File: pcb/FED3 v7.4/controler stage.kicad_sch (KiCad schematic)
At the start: 25 parts, among them IC4 RTC PCF8523T, J1 Conn_02x03_Odd_Even, SW2 SPST_TACT-KMR2, U1 ATSAMD21G18A, U4 Adafruit LCD Screen, X1 ClockXtal, X2 uXtal, X4 microsd

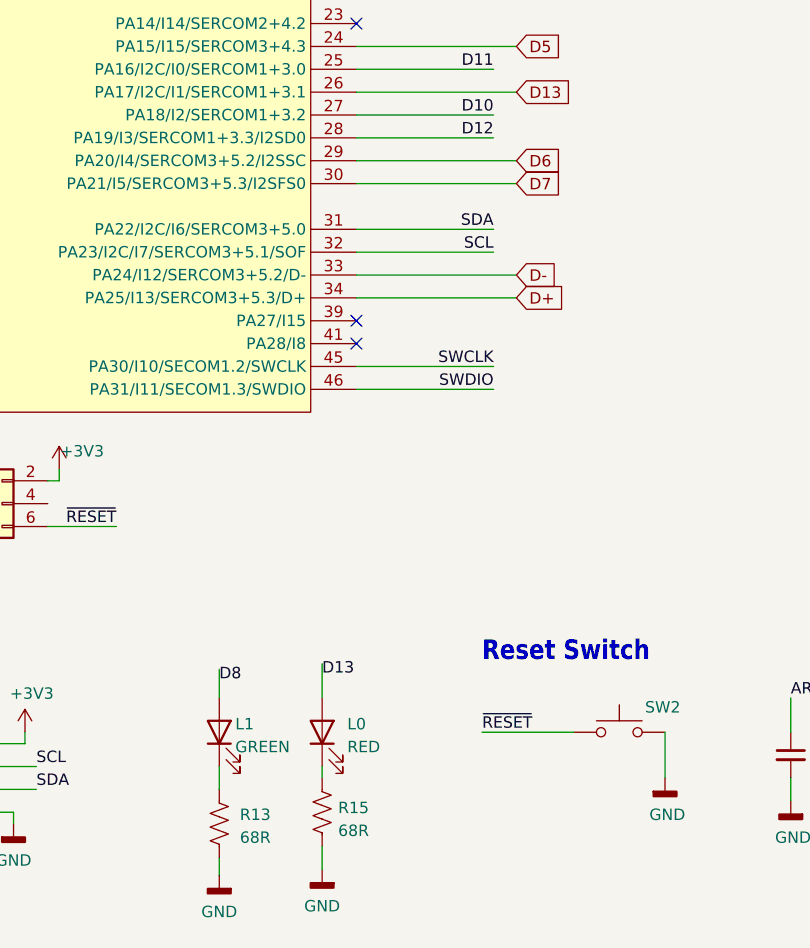
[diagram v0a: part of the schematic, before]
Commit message: v.7.4 - alterações rail power
v.7.4
- modificada estrutura rail power: VUSB apenas para Vcharging
- modificadas Rs de LEDs para diminuir I
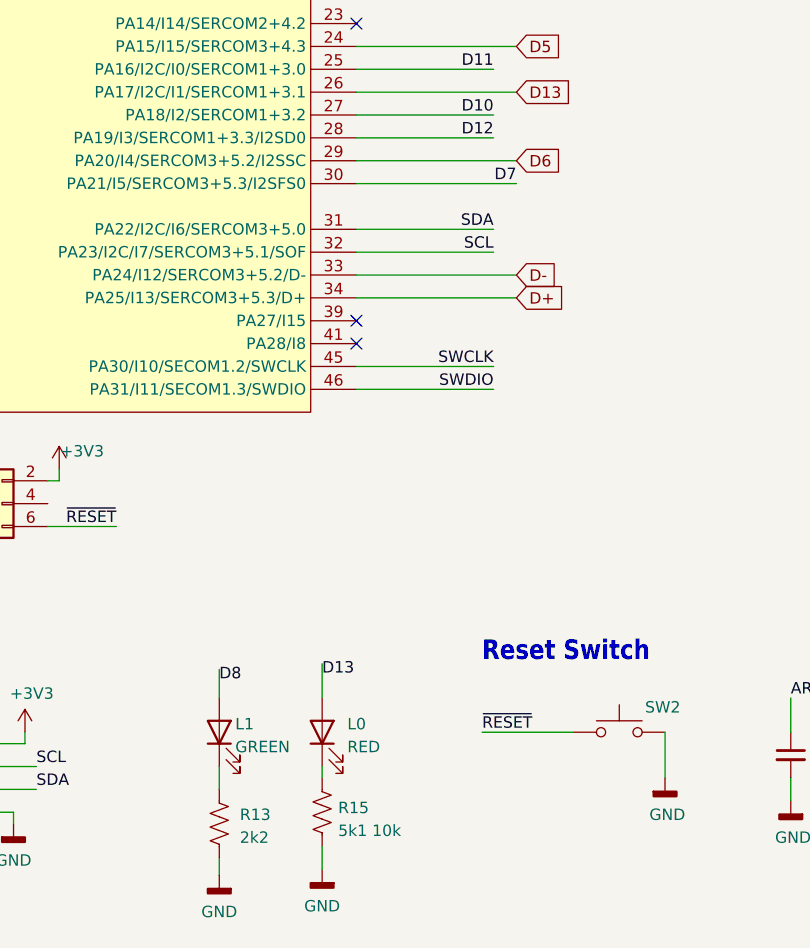
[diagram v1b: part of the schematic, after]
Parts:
- R13: value 68R -> 2k2; MPN RCS040268R0FKED -> ERJ-2RKF2201X; OEPSPN OEPS020032 -> OEPS020174
- R15: value 68R -> 5k1 10k; MPN RCS040268R0FKED -> ??; OEPSPN OEPS020032 -> TBD
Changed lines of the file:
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@@
+		)
+	)
+	(label "D7"
+		(at 138.43 100.33 180)
+		(effects
+			(font
+				(size 1.27 1.27)
+			)
+			(justify right bottom)
 		)
 	)
@@
 		)
 	)
-	(global_label "D7"
-		(shape input)
-		(at 138.43 100.33 0)
-		(fields_autoplaced yes)
-		(effects
-			(font
-				(size 1.27 1.27)
-			)
-			(justify left)
-		)
-		(property "Intersheetrefs" "${INTERSHEET_REFS}"
-			(at 143.7851 100.33 0)
-			(effects
-				(font
-					(size 1.27 1.27)
-				)
-				(justify bottom)
-				(hide yes)
-			)
-		)
-	)
 	(global_label "D6"
 		(shape input)
@@
 			)
 		)
-		(property "Value" "68R"
+		(property "Value" "5k1 10k"
 			(at 118.618 172.974 0)
 			(effects
@@
 			)
 		)
-		(property "OEPSPN" "OEPS020032"
+		(property "OEPSPN" "TBD"
 			(at 116.84 170.18 0)
 			(effects
@@
 			)
 		)
-		(property "MPN" "RCS040268R0FKED"
+		(property "MPN" "??"
 			(at 116.84 170.18 0)
 			(effects
@@
 			)
 		)
-		(property "Value" "68R"
+		(property "Value" "2k2"
 			(at 107.696 173.736 0)
 			(effects
@@
 			)
 		)
-		(property "OEPSPN" "OEPS020032"
+		(property "OEPSPN" "OEPS020174"
 			(at 105.41 171.45 0)
 			(effects
@@
 			)
 		)
-		(property "MPN" "RCS040268R0FKED"
+		(property "MPN" "ERJ-2RKF2201X"
 			(at 105.41 171.45 0)
 			(effects

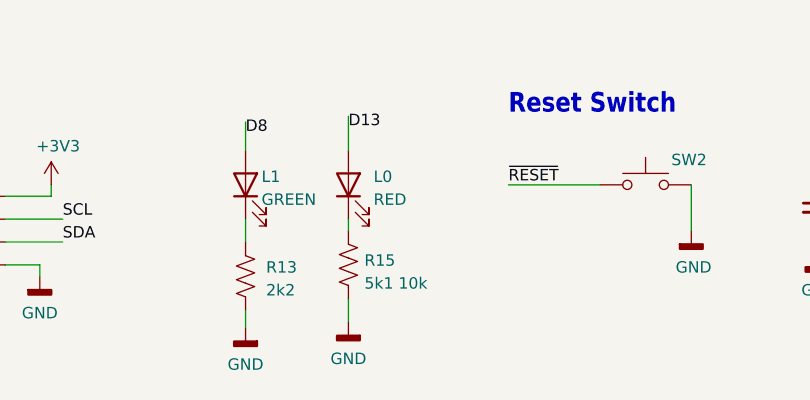
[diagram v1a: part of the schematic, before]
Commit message: v.7.4 - commit to final review
- I2C plug moved to board front side
- Rs to LEDs changed - impose less I
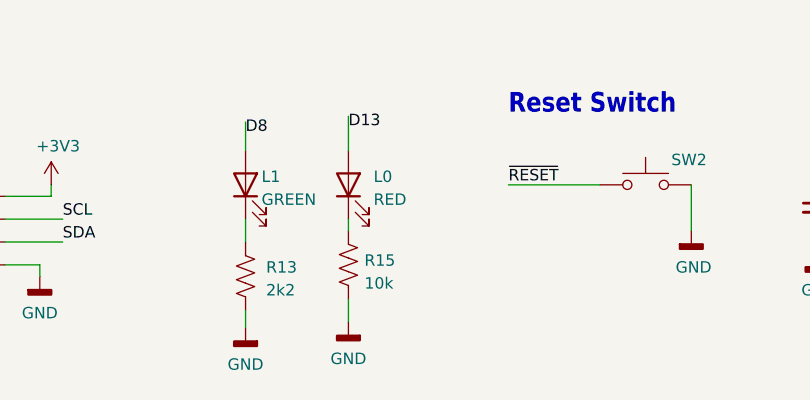
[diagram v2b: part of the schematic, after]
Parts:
- AUX_I2C0: footprint FED3_PCBLib:1X04 -> Connector_JST:JST_PH_B4B-PH-K_1x04_P2.00mm_Vertical
- R15: value 5k1 10k -> 10k; OEPSPN TBD -> OEPS020013
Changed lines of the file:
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@@
 			)
 		)
-		(property "Description" "Two pin crystal"
+		(property "Description" "Crystal 32768 KHz ±50ppm 12.5pF 90kOhms"
 			(at 130.81 39.37 0)
 			(effects
@@
 			)
 		)
-		(property "Description" ""
+		(property "Description" "SMD CER 0402 22pF 50V ±5% C0G/NP0"
 			(at 135.89 29.21 0)
 			(effects
@@
 			)
 		)
-		(property "Description" "32.768 kHz ±10ppm Crystal 12.5pF 50 kOhms"
+		(property "Description" "Crystal 32.768 kHz ±10ppm 12.5pF 50 kOhms (OEPS K01 010)"
 			(at 257.175 138.43 0)
 			(effects
@@
 			)
 		)
-		(property "Description" ""
+		(property "Description" "SMD CER 0402 1uF 25V ±10% X5R"
 			(at 41.91 63.5 0)
 			(effects
@@
 			)
 		)
-		(property "Value" "5k1 10k"
+		(property "Value" "10k"
 			(at 118.618 172.974 0)
 			(effects
@@
 			)
 		)
-		(property "Description" ""
+		(property "Description" "SMD 0402 10kΩ ±1% 0.100W"
 			(at 116.84 170.18 0)
 			(effects
@@
 			)
 		)
-		(property "OEPSPN" "TBD"
+		(property "OEPSPN" "OEPS020013"
 			(at 116.84 170.18 0)
 			(effects
@@
 			)
 		)
-		(property "Description" ""
+		(property "Description" "SMD CER 0402 22pF 50V ±5% C0G/NP0"
 			(at 125.73 29.21 0)
 			(effects
@@
 			)
 		)
-		(property "Footprint" "FED3_PCBLib:1X04"
+		(property "Footprint" "Connector_JST:JST_PH_B4B-PH-K_1x04_P2.00mm_Vertical"
 			(at 73.66 165.1 0)
 			(effects
@@
 			)
 		)
-		(property "Description" ""
+		(property "Description" "SMD 0402 2.2kΩ ±1% 0.100W"
 			(at 105.41 171.45 0)
 			(effects
@@
 			)
 		)
-		(property "Description" "Push button switch, generic, two pins"
+		(property "Description" "SWITCH TACTILE SPST-NO 0.05A 12V"
 			(at 149.86 161.29 0)
 			(effects
@@
 			)
 		)
-		(property "Description" ""
+		(property "Description" "SMD 0402 4.7kΩ ±1% 0.100W"
 			(at 207.01 139.7 0)
 			(effects
@@
 			)
 		)
-		(property "Description" "• CR1220 SMT - Digikey: 3001K-ND\n• CD2032 BAT-HLD-001 - Digikey: BAT-HLD-001-ND"
+		(property "Description" "CR1220 Battery Holders; 12mm (OEPS K01 013)"
 			(at 256.54 148.59 0)
 			(effects
@@
 			)
 		)
-		(property "Description" "Generic connector, double row, 02x03, odd/even pin numbering scheme (row 1 odd numbers, row 2 even numbers), script generated (kicad-library-utils/schlib/autogen/connector/)"
+		(property "Description" "HEADER 2.54MM straight 2x3POS"
 			(at 78.74 135.89 0)
 			(effects
@@
 			)
 		)
-		(property "Description" ""
+		(property "Description" "CONN MICRO SD CARD R/A"
 			(at 228.6 53.34 0)
 			(effects
@@
 			)
 		)
-		(property "Description" ""
+		(property "Description" "SMD 0402 1kΩ ±1% 0.100W"
 			(at 226.06 118.11 0)
 			(effects
@@
 			)
 		)
-		(property "Description" ""
+		(property "Description" "RTC CLOCK/CALENDAR I2C"
 			(at 234.95 140.97 0)
 			(effects
@@
 			)
 		)
-		(property "Description" ""
+		(property "Description" "SMD CER 0402 1uF 25V ±10% X5R"
 			(at 168.91 163.83 0)
 			(effects
@@
 			)
 		)
-		(property "Description" ""
+		(property "Description" "SMD 0402 4.7kΩ ±1% 0.100W"
 			(at 210.185 139.7 0)
 			(effects
@@
 			)
 		)
-		(property "Description" ""
+		(property "Description" "IC MCU 32BIT 256KB FLASH 48QFN"
 			(at 69.85 77.47 0)
 			(effects

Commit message: FED3 v7.3 - 2nd revision
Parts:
- AUX_I2C0: value DNP -> TBD; footprint Connector_JST:JST_PH_B4B-PH-K_1x04_P2.00mm_Vertical -> Connector_JST:JST_SH_BM04B-SRSS-TB_1x04-1MP_P1.00mm_Vertical; OEPSPN n.a. -> TBD; now in the parts list
- R15: MPN ?? -> ERJ-2RKF1002X
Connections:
- net +3V3: now also AUX_I2C0.2 (Pin_2); no longer AUX_I2C0.1 (Pin_1)
- net GND: now also AUX_I2C0.1 (Pin_1); no longer AUX_I2C0.4 (Pin_4)
- net SCL: now also AUX_I2C0.4 (Pin_4); no longer AUX_I2C0.2 (Pin_2)
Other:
- moved on the sheet: AUX_I2C0, U4
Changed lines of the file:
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@@
 	(wire
 		(pts
-			(xy 120.65 100.33) (xy 138.43 100.33)
+			(xy 120.65 100.33) (xy 135.89 100.33)
 		)
 		(stroke
@@
 	(wire
 		(pts
-			(xy 78.74 167.64) (xy 85.09 167.64)
+			(xy 76.2 166.37) (xy 82.55 166.37)
 		)
 		(stroke
@@
 	(wire
 		(pts
+			(xy 77.47 168.91) (xy 76.2 168.91)
+		)
+		(stroke
+			(width 0)
+			(type solid)
+		)
+	)
+	(wire
+		(pts
 			(xy 41.91 120.65) (xy 44.45 120.65)
 		)
@@
 	(wire
 		(pts
-			(xy 78.74 165.1) (xy 85.09 165.1)
+			(xy 76.2 163.83) (xy 82.55 163.83)
 		)
 		(stroke
@@
 	(wire
 		(pts
+			(xy 77.47 170.18) (xy 77.47 168.91)
+		)
+		(stroke
+			(width 0)
+			(type solid)
+		)
+	)
+	(wire
+		(pts
 			(xy 205.74 73.66) (xy 205.74 76.2)
 		)
@@
 	(wire
 		(pts
-			(xy 78.74 170.18) (xy 82.55 170.18)
+			(xy 76.2 171.45) (xy 80.01 171.45)
 		)
 		(stroke
@@
 	(wire
 		(pts
-			(xy 83.82 161.29) (xy 83.82 162.56)
-		)
-		(stroke
-			(width 0)
-			(type solid)
-		)
-	)
-	(wire
-		(pts
 			(xy 250.19 153.67) (xy 250.19 146.05)
 		)
@@
 	(wire
 		(pts
-			(xy 83.82 162.56) (xy 78.74 162.56)
+			(xy 81.28 170.18) (xy 77.47 170.18)
 		)
 		(stroke
@@
 	(wire
 		(pts
-			(xy 82.55 170.18) (xy 82.55 171.45)
+			(xy 80.01 171.45) (xy 80.01 172.72)
 		)
 		(stroke
@@
 	(wire
 		(pts
-			(xy 120.65 49.53) (xy 134.62 49.53)
+			(xy 120.65 49.53) (xy 135.89 49.53)
 		)
 		(stroke
@@
 	)
 	(label "SDA"
-		(at 85.09 167.64 0)
+		(at 82.55 166.37 0)
 		(effects
 			(font
@@
 	)
 	(label "SCL"
-		(at 85.09 165.1 0)
+		(at 82.55 163.83 0)
 		(effects
 			(font
@@
 	)
 	(label "AREF"
-		(at 134.62 49.53 180)
+		(at 135.89 49.53 180)
 		(effects
 			(font
@@
 	)
 	(label "~{RESET}"
-		(at 34.29 44.45 180)
+		(at 34.29 44.45 0)
 		(effects
 			(font
 				(size 1.27 1.27)
 			)
-			(justify right bottom)
+			(justify left bottom)
 		)
 	)
@@
 	)
 	(label "D1"
-		(at 132.08 69.85 180)
+		(at 135.89 69.85 180)
 		(effects
 			(font
@@
 	)
 	(label "D0"
-		(at 132.08 72.39 180)
+		(at 135.89 72.39 180)
 		(effects
 			(font
@@
 	)
 	(label "D7"
-		(at 138.43 100.33 180)
+		(at 135.89 100.33 180)
 		(effects
 			(font
@@
 			)
 		)
-		(property "MPN" "??"
+		(property "MPN" "ERJ-2RKF1002X"
 			(at 116.84 170.18 0)
 			(effects
@@
 	(symbol
 		(lib_id "Connector_Generic:Conn_01x04")
-		(at 73.66 165.1 0)
-		(mirror y)
+		(at 71.12 168.91 180)
 		(unit 1)
 		(exclude_from_sim no)
-		(in_bom no)
+		(in_bom yes)
 		(on_board yes)
 		(dnp no)
-		(fields_autoplaced yes)
 		(property "Reference" "AUX_I2C0"
-			(at 73.66 158.75 0)
+			(at 72.644 160.02 0)
 			(effects
 				(font
 					(size 1.27 1.27)
 				)
-				(justify bottom)
 			)
 		)
-		(property "Value" "DNP"
-			(at 80.01 172.72 0)
+		(property "Value" "TBD"
+			(at 77.47 161.29 0)
 			(effects
 				(font
@@
 			)
 		)
-		(property "Footprint" "Connector_JST:JST_PH_B4B-PH-K_1x04_P2.00mm_Vertical"
-			(at 73.66 165.1 0)
+		(property "Footprint" "Connector_JST:JST_SH_BM04B-SRSS-TB_1x04-1MP_P1.00mm_Vertical"
+			(at 71.12 168.91 0)
 			(effects
 				(font
@@
 			)
 		)
-		(property "Datasheet" ""
-			(at 73.66 165.1 0)
+		(property "Datasheet" "~"
+			(at 71.12 168.91 0)
 			(effects
 				(font
@@
 		)
 		(property "Description" "Generic connector, single row, 01x04, script generated (kicad-library-utils/schlib/autogen/connector/)"
-			(at 73.66 165.1 0)
+			(at 71.12 168.91 0)
 			(effects
 				(font
@@
 			)
 		)
-		(property "OEPSPN" "n.a."
-			(at 73.66 165.1 0)
+		(property "OEPSPN" "TBD"
+			(at 71.12 168.91 0)
 			(effects
 				(font
@@
 		)
 		(property "MPN" "n.a."
-			(at 73.66 165.1 0)
+			(at 71.12 168.91 0)
 			(effects
 				(font
@@
 	(symbol
 		(lib_id "power:GNDD")
-		(at 82.55 171.45 0)
+		(at 80.01 172.72 0)
 		(unit 1)
 		(exclude_from_sim no)
@@
 		(dnp no)
 		(property "Reference" "#PWR050"
-			(at 82.55 171.45 0)
+			(at 80.01 172.72 0)
 			(effects
 				(font
@@
 		)
 		(property "Value" "GND"
-			(at 82.55 176.276 0)
+			(at 80.01 177.546 0)
 			(effects
 				(font
@@
 		)
 		(property "Footprint" ""
-			(at 82.55 171.45 0)
+			(at 80.01 172.72 0)
 			(effects
 				(font
@@
 		)
 		(property "Datasheet" ""
-			(at 82.55 171.45 0)
+			(at 80.01 172.72 0)
 			(effects
 				(font
@@
 		)
 		(property "Description" "Power symbol creates a global label with name \"GNDD\" , digital ground"
-			(at 82.55 171.45 0)
+			(at 80.01 172.72 0)
 			(effects
 				(font
@@
 	(symbol
 		(lib_id "power:+3V3")
-		(at 83.82 161.29 0)
+		(at 81.28 170.18 0)
 		(unit 1)
 		(exclude_from_sim no)
@@
 		(dnp no)
 		(property "Reference" "#+3V07"
-			(at 83.82 161.29 0)
+			(at 81.28 170.18 0)
 			(effects
 				(font
@@
 		)
 		(property "Value" "+3V3"
-			(at 84.582 157.734 0)
+			(at 84.582 169.164 0)
 			(effects
 				(font
@@
 		)
 		(property "Footprint" ""
-			(at 83.82 161.29 0)
+			(at 81.28 170.18 0)
 			(effects
 				(font
@@
 		)
 		(property "Datasheet" ""
-			(at 83.82 161.29 0)
+			(at 81.28 170.18 0)
 			(effects
 				(font
@@
 		)
 		(property "Description" ""
-			(at 83.82 161.29 0)
+			(at 81.28 170.18 0)
 			(effects
 				(font
@@
 	(symbol
 		(lib_id "FED3 SymbLib:LCD_SCREEN")
-		(at 27.94 154.94 0)
+		(at 24.13 172.72 0)
 		(unit 1)
 		(exclude_from_sim no)
@@
 		(dnp no)
 		(property "Reference" "U4"
-			(at 18.796 136.906 0)
+			(at 14.986 154.686 0)
 			(effects
 				(font
@@
 		)
 		(property "Value" "Adafruit LCD Screen"
-			(at 18.796 139.446 0)
+			(at 14.986 157.226 0)
 			(effects
 				(font
@@
 		)
 		(property "Footprint" ""
-			(at 27.94 154.94 0)
+			(at 24.13 172.72 0)
 			(effects
 				(font
@@
 		)
 		(property "Datasheet" ""
-			(at 27.94 154.94 0)
+			(at 24.13 172.72 0)
 			(effects
 				(font
@@
 		)
 		(property "Description" ""
-			(at 27.94 154.94 0)
+			(at 24.13 172.72 0)
 			(effects
 				(font
@@
 		)
 		(property "OEPSPN" "TBD"
-			(at 21.082 171.958 0)
+			(at 17.272 189.738 0)
 			(effects
 				(font
@@
 		)
 		(property "MPN" "3502"
-			(at 27.94 154.94 0)
+			(at 24.13 172.72 0)
 			(effects
 				(font

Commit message: retomar sincronia PCB com main-branch @12Junho
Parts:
- AUX_I2C0: value TBD -> Qwiic; MPN n.a. -> BM04B-SRSS-TB(LF)(SN); OEPSPN TBD -> OEPS070125
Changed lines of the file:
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@@
 			)
 		)
-		(property "Value" "TBD"
+		(property "Value" "Qwiic"
 			(at 77.47 161.29 0)
 			(effects
@@
 			)
 		)
-		(property "OEPSPN" "TBD"
+		(property "OEPSPN" "OEPS070125"
 			(at 71.12 168.91 0)
 			(effects
@@
 			)
 		)
-		(property "MPN" "n.a."
+		(property "MPN" "BM04B-SRSS-TB(LF)(SN)"
 			(at 71.12 168.91 0)
 			(effects

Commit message: actualizados ficheiros produção
- modificadas props de componentes para agilizar o criar ficheiros de produção
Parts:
- SCREEN0: MPN 61300611021 -> _ acrescentar PN ecrã ou header 90º?; OEPSPN OEPS070118 -> _ acrescentar PN ecrã ou header 90º?
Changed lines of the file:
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@@
 			)
 		)
-		(property "OEPSPN" "OEPS070118"
+		(property "OEPSPN" "_ acrescentar PN ecrã ou header 90º?"
 			(at 38.1 167.64 0)
 			(effects
@@
 			)
 		)
-		(property "MPN" "61300611021"
+		(property "MPN" "_ acrescentar PN ecrã ou header 90º?"
 			(at 38.1 167.64 0)
 			(effects

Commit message: getting tunned with Jonathan review #13
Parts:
- SCREEN0: MPN _ acrescentar PN ecrã ou header 90º? -> 61300611021; OEPSPN _ acrescentar PN ecrã ou header 90º? -> OEPS070118
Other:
- company: (none) -> Kravitz Lab
- title: (none) -> FED3 Control Board
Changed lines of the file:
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@@
 	(generator_version "9.0")
 	(paper "A4")
+	(title_block
+		(title "FED3 Control Board")
+		(rev "7.4")
+		(company "Kravitz Lab")
+		(comment 1 "Open Ephys, Inc.")
+	)
 	(text "MICROSD CARD"
 		(exclude_from_sim no)
@@
 			)
 		)
-		(property "OEPSPN" "_ acrescentar PN ecrã ou header 90º?"
+		(property "OEPSPN" "OEPS070118"
 			(at 38.1 167.64 0)
 			(effects
@@
 			)
 		)
-		(property "MPN" "_ acrescentar PN ecrã ou header 90º?"
+		(property "MPN" "61300611021"
 			(at 38.1 167.64 0)
 			(effects
